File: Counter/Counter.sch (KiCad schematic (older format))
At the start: 40 parts, among them J1 Conn_01x16, J2 Conn_01x16, J3 Conn_01x16, J4 Conn_01x16, U1 74LS00, U10 74LS245, U2 74LS04, U4 74LS161, U5 74LS161, U6 74LS161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

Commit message: Fixed floating inputs; improved power; added parts list; replaced JK latches
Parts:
- added unit 3 of U1
- added unit 4 of U1
- added unit 4 of U2
- added unit 5 of U2
- added unit 6 of U2
- RN1, RN2: value 100k -> 1k
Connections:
- net GND: now also U1.10, U1.12, U1.13, U1.9, U2.11, U2.13, U2.9
- no-connect marks 1 -> 6
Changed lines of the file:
@@
 P 1500 7250
 F 0 "RN1" H 1020 7204 50  0000 R CNN
-F 1 "100k" H 1020 7295 50  0000 R CNN
+F 1 "1k" H 1020 7295 50  0000 R CNN
 F 2 "Resistor_THT:R_Array_SIP9" V 1975 7250 50  0001 C CNN
 F 3 "http://www.vishay.com/docs/31509/csc.pdf" H 1500 7250 50  0001 C CNN
@@
 P 2700 7250
 F 0 "RN2" H 2220 7204 50  0000 R CNN
-F 1 "100k" H 2220 7295 50  0000 R CNN
+F 1 "1k" H 2220 7295 50  0000 R CNN
 F 2 "Resistor_THT:R_Array_SIP9" V 3175 7250 50  0001 C CNN
 F 3 "http://www.vishay.com/docs/31509/csc.pdf" H 2700 7250 50  0001 C CNN
@@
 	1    0    0    -1
 $EndComp
+$Comp
+L 74xx:74LS04 U2
+U 4 1 607EDE23
+P 10250 5000
+F 0 "U2" H 10250 5317 50  0000 C CNN
+F 1 "74LS04" H 10250 5226 50  0000 C CNN
+F 2 "Package_DIP:DIP-14_W7.62mm" H 10250 5000 50  0001 C CNN
+F 3 "http://www.ti.com/lit/gpn/sn74LS04" H 10250 5000 50  0001 C CNN
+	4    10250 5000
+	1    0    0    -1
+$EndComp
+$Comp
+L 74xx:74LS04 U2
+U 5 1 607EF49E
+P 10250 5500
+F 0 "U2" H 10250 5817 50  0000 C CNN
+F 1 "74LS04" H 10250 5726 50  0000 C CNN
+F 2 "Package_DIP:DIP-14_W7.62mm" H 10250 5500 50  0001 C CNN
+F 3 "http://www.ti.com/lit/gpn/sn74LS04" H 10250 5500 50  0001 C CNN
+	5    10250 5500
+	1    0    0    -1
+$EndComp
+$Comp
+L 74xx:74LS04 U2
+U 6 1 607F1889
+P 10250 6000
+F 0 "U2" H 10250 6317 50  0000 C CNN
+F 1 "74LS04" H 10250 6226 50  0000 C CNN
+F 2 "Package_DIP:DIP-14_W7.62mm" H 10250 6000 50  0001 C CNN
+F 3 "http://www.ti.com/lit/gpn/sn74LS04" H 10250 6000 50  0001 C CNN
+	6    10250 6000
+	1    0    0    -1
+$EndComp
+Text GLabel 9850 5000 0    50   Input ~ 0
+GND
+Wire Wire Line
+	9850 5000 9950 5000
+Text GLabel 9850 5500 0    50   Input ~ 0
+GND
+Wire Wire Line
+	9850 5500 9950 5500
+Text GLabel 9850 6000 0    50   Input ~ 0
+GND
+Wire Wire Line
+	9850 6000 9950 6000
+NoConn ~ 10550 5000
+NoConn ~ 10550 5500
+NoConn ~ 10550 6000
+$Comp
+L 74xx:74LS00 U1
+U 3 1 608BA8BA
+P 10350 1250
+F 0 "U1" H 10350 1575 50  0000 C CNN
+F 1 "74LS00" H 10350 1484 50  0000 C CNN
+F 2 "Package_DIP:DIP-14_W7.62mm" H 10350 1250 50  0001 C CNN
+F 3 "http://www.ti.com/lit/gpn/sn74ls00" H 10350 1250 50  0001 C CNN
+	3    10350 1250
+	1    0    0    -1
+$EndComp
+$Comp
+L 74xx:74LS00 U1
+U 4 1 608BDA9C
+P 10350 1850
+F 0 "U1" H 10350 2175 50  0000 C CNN
+F 1 "74LS00" H 10350 2084 50  0000 C CNN
+F 2 "Package_DIP:DIP-14_W7.62mm" H 10350 1850 50  0001 C CNN
+F 3 "http://www.ti.com/lit/gpn/sn74ls00" H 10350 1850 50  0001 C CNN
+	4    10350 1850
+	1    0    0    -1
+$EndComp
+Wire Wire Line
+	10050 1150 10050 1250
+Wire Wire Line
+	10050 1750 10050 1850
+Wire Wire Line
+	10050 1250 9950 1250
+Connection ~ 10050 1250
+Wire Wire Line
+	10050 1250 10050 1350
+Wire Wire Line
+	10050 1850 9950 1850
+Connection ~ 10050 1850
+Wire Wire Line
+	10050 1850 10050 1950
+Text GLabel 9950 1850 0    50   Input ~ 0
+GND
+Text GLabel 9950 1250 0    50   Input ~ 0
+GND
+NoConn ~ 10650 1250
+NoConn ~ 10650 1850
 $EndSCHEMATC

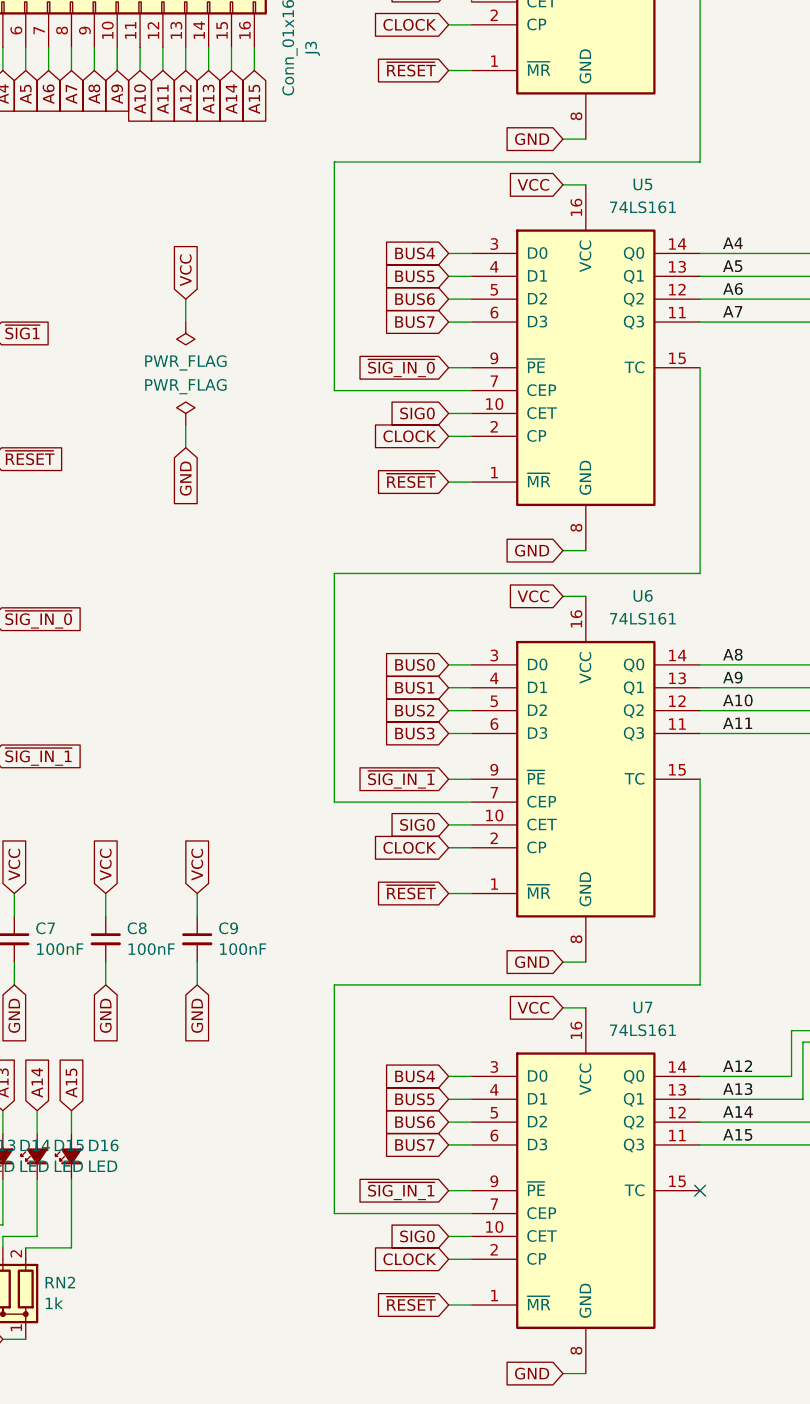
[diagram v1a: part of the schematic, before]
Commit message: Fix reversed headers on ALU, and counting issues on counter (CET / CEP connections)
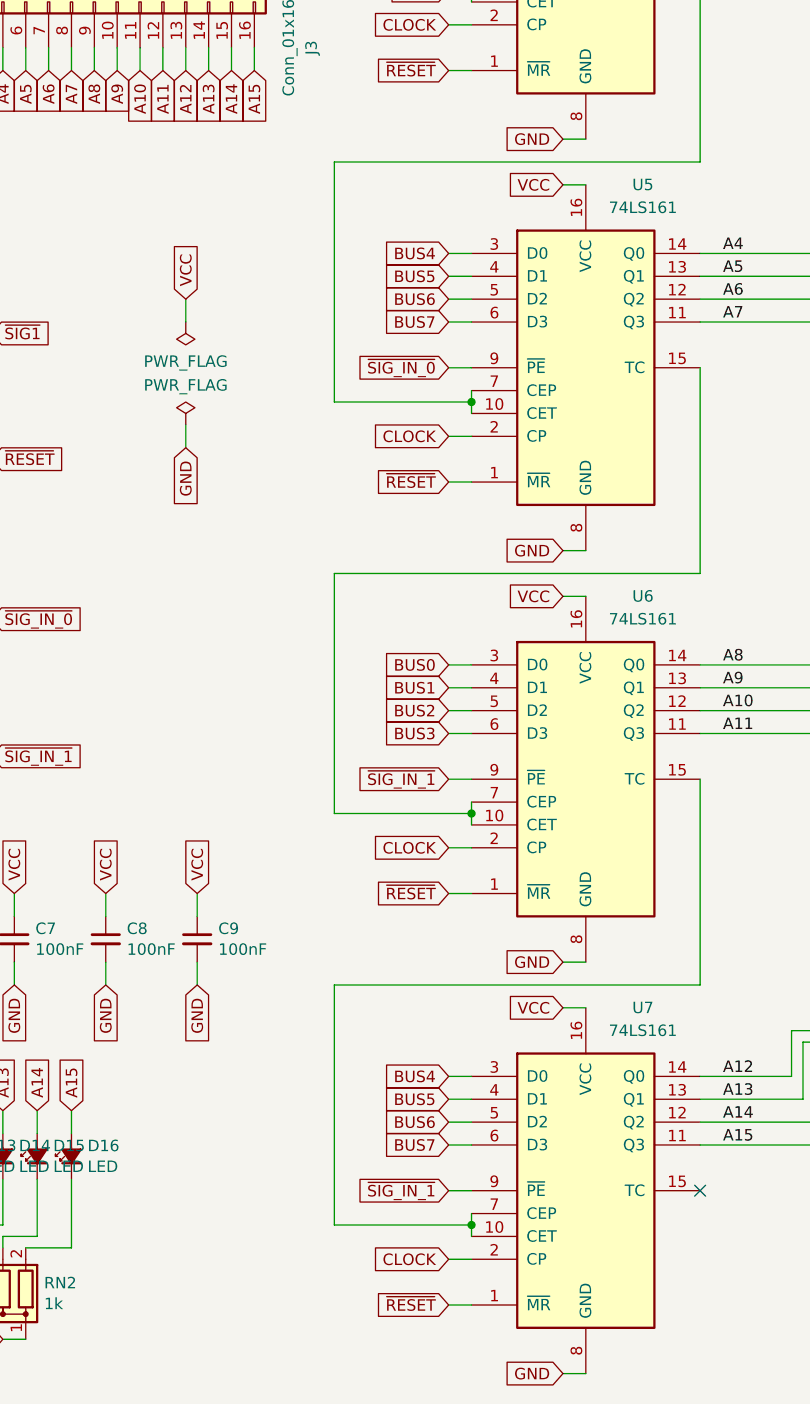
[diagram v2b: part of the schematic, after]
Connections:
- net SIG0: no longer U5.10 (CET), U6.10 (CET), U7.10 (CET)
- net at U4.15 (TC), U5.7 (CEP): now also U5.10 (CET)
- net at U5.15 (TC), U6.7 (CEP): now also U6.10 (CET)
- net at U6.15 (TC), U7.7 (CEP): now also U7.10 (CET)
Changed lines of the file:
@@
 	6050 3200 6050 4100
 Wire Wire Line
-	4450 4100 4450 5100
-Wire Wire Line
 	6050 5000 6050 5900
 Wire Wire Line
 	6050 5900 4450 5900
-Wire Wire Line
-	4450 5900 4450 6900
 Text Label 6150 4500 0    50   ~ 0
 A8
@@
 	5050 1550 5050 1600
 Connection ~ 5050 1550
-Text GLabel 4950 3400 0    50   Input ~ 0
-SIG0
-Wire Wire Line
-	4950 3400 5050 3400
-Wire Wire Line
-	4450 3300 5050 3300
-Wire Wire Line
-	4450 2300 4450 3300
-Wire Wire Line
-	4450 5100 5050 5100
-Text GLabel 4950 5200 0    50   Input ~ 0
-SIG0
-Wire Wire Line
-	4950 5200 5050 5200
-Text GLabel 4950 7000 0    50   Input ~ 0
-SIG0
-Wire Wire Line
-	4950 7000 5050 7000
-Wire Wire Line
-	4450 6900 5050 6900
 Text GLabel 4950 1700 0    50   Input ~ 0
 CLOCK
@@
 NoConn ~ 10650 1250
 NoConn ~ 10650 1850
+Wire Wire Line
+	5050 7000 5050 6950
+Wire Wire Line
+	5050 6950 4450 6950
+Wire Wire Line
+	4450 5900 4450 6950
+Connection ~ 5050 6950
+Wire Wire Line
+	5050 6950 5050 6900
+Wire Wire Line
+	5050 5200 5050 5150
+Wire Wire Line
+	5050 5150 4450 5150
+Wire Wire Line
+	4450 4100 4450 5150
+Connection ~ 5050 5150
+Wire Wire Line
+	5050 5150 5050 5100
+Wire Wire Line
+	5050 3400 5050 3350
+Wire Wire Line
+	5050 3350 4450 3350
+Wire Wire Line
+	4450 2300 4450 3350
+Connection ~ 5050 3350
+Wire Wire Line
+	5050 3350 5050 3300
 $EndSCHEMATC

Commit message: Update all boards to r3, and update revision log and gitignore
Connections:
- net A0: now also D16.2 (A); no longer D1.2 (A)
- net A1: now also D15.2 (A); no longer D2.2 (A)
- net A10: now also D6.2 (A); no longer D11.2 (A)
- net A11: now also D5.2 (A); no longer D12.2 (A)
- net A12: now also D4.2 (A); no longer D13.2 (A)
- net A13: now also D3.2 (A); no longer D14.2 (A)
- net A14: now also D2.2 (A); no longer D15.2 (A)
- net A15: now also D1.2 (A); no longer D16.2 (A)
- net A2: now also D14.2 (A); no longer D3.2 (A)
- net A3: now also D13.2 (A); no longer D4.2 (A)
- net A4: now also D12.2 (A); no longer D5.2 (A)
- net A5: now also D11.2 (A); no longer D6.2 (A)
- net A6: now also D10.2 (A); no longer D7.2 (A)
- net A7: now also D9.2 (A); no longer D8.2 (A)
- net A8: now also D8.2 (A); no longer D9.2 (A)
- net A9: now also D7.2 (A); no longer D10.2 (A)
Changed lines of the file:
@@
 	0    -1   -1   0
 $EndComp
+Text GLabel 3300 6450 1    50   Input ~ 0
+A0
+Text GLabel 3150 6450 1    50   Input ~ 0
+A1
+Text GLabel 3000 6450 1    50   Input ~ 0
+A2
+Text GLabel 2850 6450 1    50   Input ~ 0
+A3
+Text GLabel 2700 6450 1    50   Input ~ 0
+A4
+Text GLabel 2550 6450 1    50   Input ~ 0
+A5
+Text GLabel 2400 6450 1    50   Input ~ 0
+A6
+Text GLabel 2250 6450 1    50   Input ~ 0
+A7
+Text GLabel 2100 6450 1    50   Input ~ 0
+A8
+Text GLabel 1950 6450 1    50   Input ~ 0
+A9
+Text GLabel 1800 6450 1    50   Input ~ 0
+A10
+Text GLabel 1650 6450 1    50   Input ~ 0
+A11
+Text GLabel 1500 6450 1    50   Input ~ 0
+A12
+Text GLabel 1350 6450 1    50   Input ~ 0
+A13
+Text GLabel 1200 6450 1    50   Input ~ 0
+A14
 Text GLabel 1050 6450 1    50   Input ~ 0
-A0
-Text GLabel 1200 6450 1    50   Input ~ 0
-A1
-Text GLabel 1350 6450 1    50   Input ~ 0
-A2
-Text GLabel 1500 6450 1    50   Input ~ 0
-A3
-Text GLabel 1650 6450 1    50   Input ~ 0
-A4
-Text GLabel 1800 6450 1    50   Input ~ 0
-A5
-Text GLabel 1950 6450 1    50   Input ~ 0
-A6
-Text GLabel 2100 6450 1    50   Input ~ 0
-A7
-Text GLabel 2250 6450 1    50   Input ~ 0
-A8
-Text GLabel 2400 6450 1    50   Input ~ 0
-A9
-Text GLabel 2550 6450 1    50   Input ~ 0
-A10
-Text GLabel 2700 6450 1    50   Input ~ 0
-A11
-Text GLabel 2850 6450 1    50   Input ~ 0
-A12
-Text GLabel 3000 6450 1    50   Input ~ 0
-A13
-Text GLabel 3150 6450 1    50   Input ~ 0
-A14
-Text GLabel 3300 6450 1    50   Input ~ 0
 A15
 Wire Wire Line
